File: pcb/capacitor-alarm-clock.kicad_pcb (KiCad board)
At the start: 2 copper layers, 62.3 x 64.3 mm, 94 parts

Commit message: Change input voltage range
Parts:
- R12, R15, R18: value 10R -> 5R1
- R9: value 200K -> 100K
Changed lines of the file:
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@@
 			)
 		)
-		(property "Value" "200K"
+		(property "Value" "100K"
 			(at 0 1.43 0)
 			(layer "F.Fab")
@@
 			)
 		)
-		(property "Supplier Part" "C105574"
+		(property "Supplier Part" "C2906980"
 			(at 0 0 180)
 			(unlocked yes)
@@
 			)
 		)
-		(property "Value" "10R"
+		(property "Value" "5R1"
 			(at 10.16 -1.5 90)
 			(layer "F.Fab")
@@
 			)
 		)
-		(property "Value" "10R"
+		(property "Value" "5R1"
 			(at 10.16 -1.5 90)
 			(layer "F.Fab")
@@
 			)
 		)
-		(property "Value" "10R"
+		(property "Value" "5R1"
 			(at 10.16 -1.5 90)
 			(layer "F.Fab")

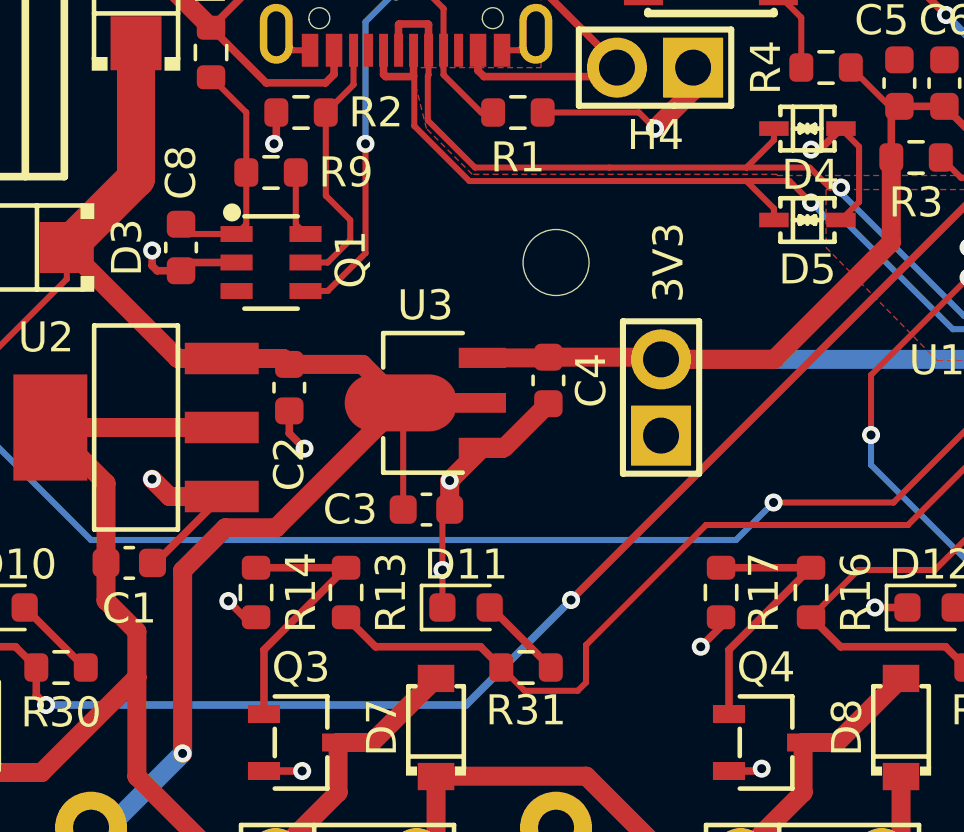
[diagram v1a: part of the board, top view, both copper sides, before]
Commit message: Improve voltage regulator circuit so it doesn't keep browning out
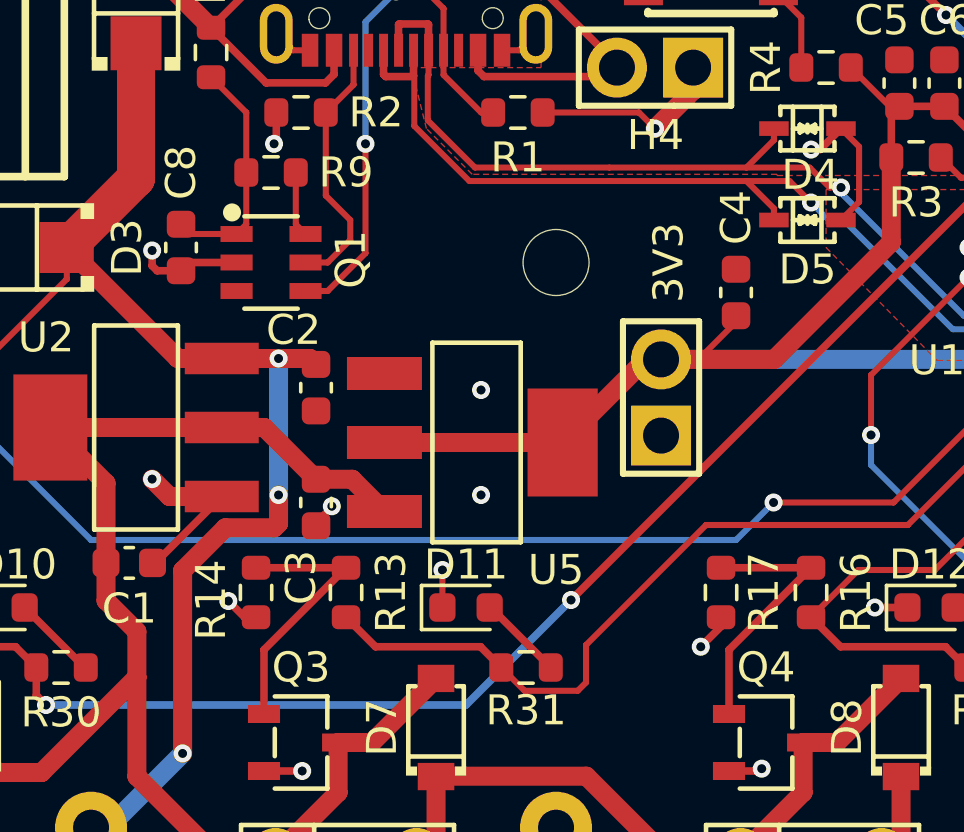
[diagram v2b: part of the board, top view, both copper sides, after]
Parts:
- removed U3: ~, EasyEDA_Lib:SOT-89-3_L4.5-W2.5-P1.50-LS4.2-BR
- added U5: ~, EasyEDA_Lib:SOT-223-3_L6.5-W3.4-P2.30-LS7.0-BR-1, F.Cu at (44.8, 44.5)
- moved C4 6.91 mm to (53.5, 39.5), turned to 90 degrees
- moved C3 3.69 mm to (39.5, 46.5), turned to -90 degrees
- moved C2 0.89 mm to (39.5, 42.7)
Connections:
- C3 pad 1: VCC -> Vdrive
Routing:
- net GND: track 122.9 -> 114.8 mm, vias 36 -> 37
- net VCC: track 95.3 -> 88.1 mm, vias 1 -> 3
- net Vdrive: track 63.1 -> 69.7 mm
- net +3V3: track 66.6 -> 73.1 mm
